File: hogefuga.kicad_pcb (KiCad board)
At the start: 2 copper layers, 95.3 x 97.6 mm, 45 parts, among them J1 MJ-4PP-9, SW1 SW_PUSH, SW10 SW_PUSH, SW11 SW_PUSH, SW12 SW_PUSH, SW13 SW_PUSH, SW14 SW_PUSH, SW15 SW_PUSH, SW16 SW_PUSH, SW17 SW_PUSH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

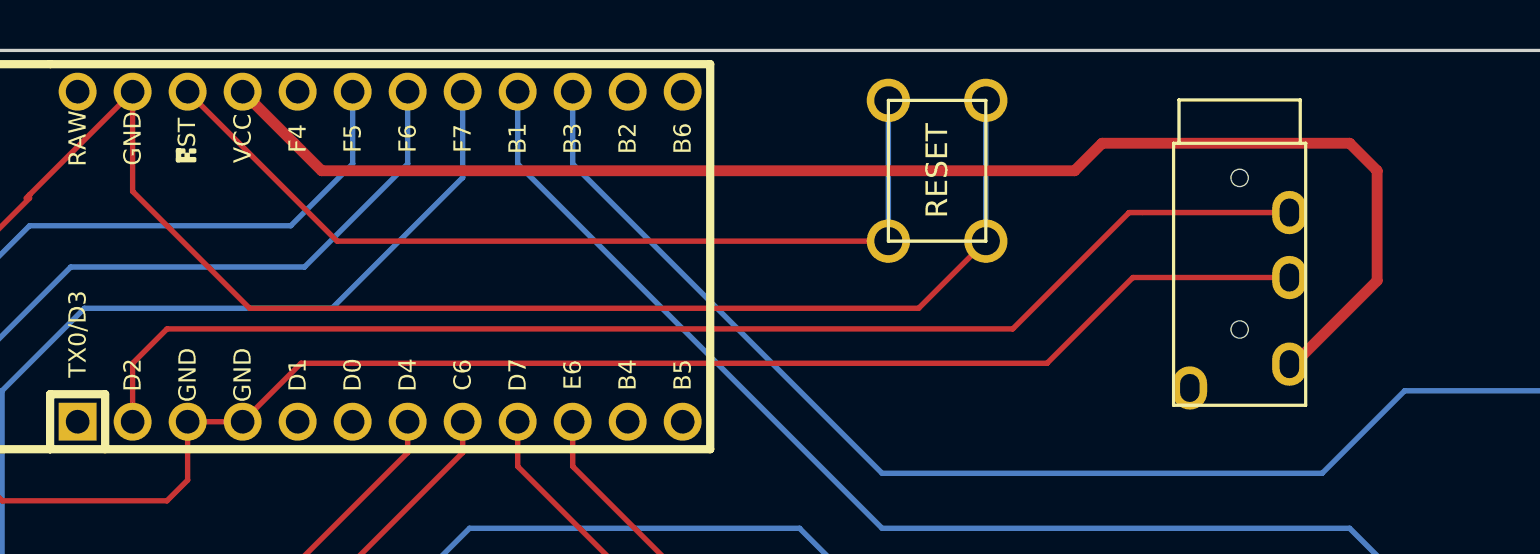
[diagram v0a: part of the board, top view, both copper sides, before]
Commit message: jack moved
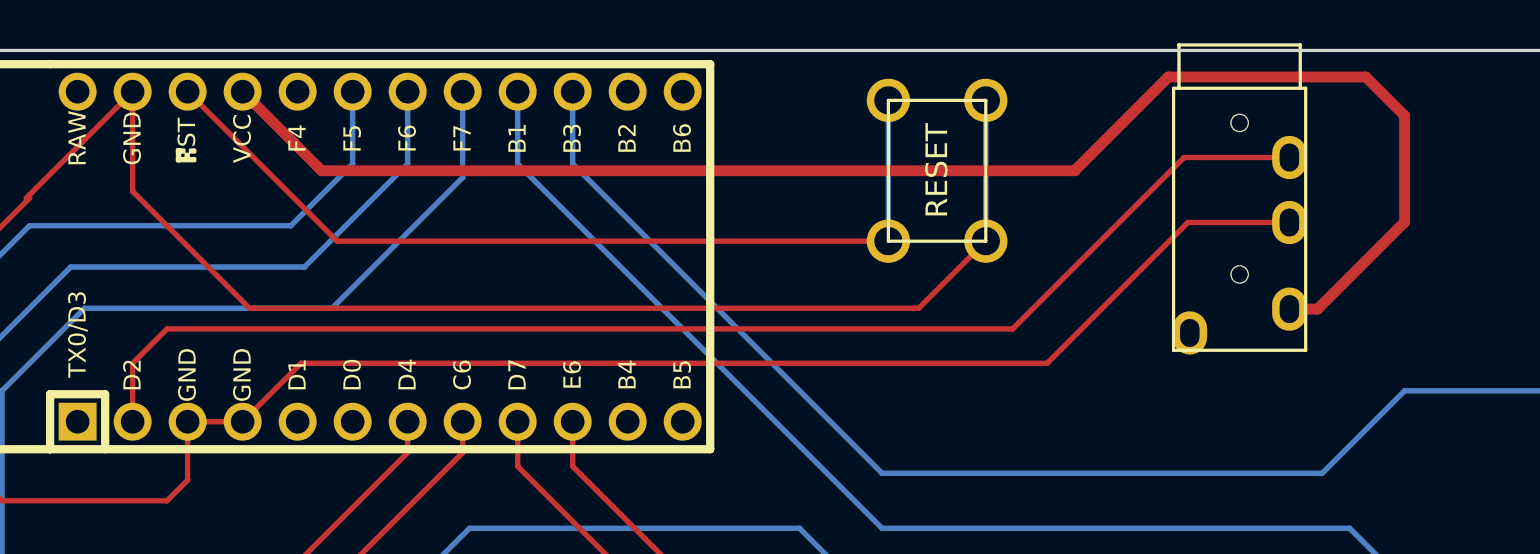
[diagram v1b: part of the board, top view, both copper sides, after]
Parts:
- moved J1 2.54 mm to (120.7, 27.9)
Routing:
- net VCC: track 65.7 -> 69.6 mm
- net data: track 59.0 -> 60.1 mm
- net GND: track 144.1 -> 145.1 mm
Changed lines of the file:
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@@
     (thickness 1.6)
     (drawings 10)
-    (tracks 372)
+    (tracks 371)
     (zones 0)
     (modules 45)
@@
   )
   (setup
-    (last_trace_width 0.25)
+    (last_trace_width 0.5)
     (user_trace_width 0.5)
     (trace_clearance 0.2)
@@
   )
   (module lib:Keebio-PJ-320A (layer F.Cu)
-    (at 120.65 30.48)
+    (at 120.65 27.94)
     (fp_text reference J1 (at 0 14.2) (layer Dwgs.User)
       (effects (font (size 1 1) (thickness 0.15)))
@@
   (segment (start 64.77 33.02) (end 59.69 38.1) (width 0.25) (layer F.Cu) (net 30))
   (segment (start 59.69 43.18) (end 59.69 38.1) (width 0.25) (layer F.Cu) (net 30))
-  (segment (start 115.72 36.68) (end 122.95 36.68) (width 0.25) (layer F.Cu) (net 30) (status 20))
   (segment (start 108.93 35) (end 108.93 28.5) (width 0.25) (layer B.Cu) (net 30))
-  (segment (start 74.6125 43.33875) (end 77.31125 40.64) (width 0.25) (layer F.Cu) (net 30))
-  (segment (start 77.31125 40.64) (end 111.76 40.64) (width 0.25) (layer F.Cu) (net 30))
-  (segment (start 111.76 40.64) (end 115.72 36.68) (width 0.25) (layer F.Cu) (net 30))
   (segment (start 69.5325 32.7025) (end 69.5325 28.09875) (width 0.25) (layer F.Cu) (net 30))
   (segment (start 74.93 38.1) (end 69.5325 32.7025) (width 0.25) (layer F.Cu) (net 30))
   (segment (start 108.93 35) (end 105.83 38.1) (width 0.25) (layer F.Cu) (net 30))
   (segment (start 105.83 38.1) (end 74.93 38.1) (width 0.25) (layer F.Cu) (net 30))
+  (segment (start 111.76 40.64) (end 118.26 34.14) (width 0.25) (layer F.Cu) (net 30))
+  (segment (start 118.26 34.14) (end 122.95 34.14) (width 0.25) (layer F.Cu) (net 30))
+  (segment (start 74.6125 43.33875) (end 77.31125 40.64) (width 0.25) (layer F.Cu) (net 30))
+  (segment (start 77.31125 40.64) (end 111.76 40.64) (width 0.25) (layer F.Cu) (net 30))
   (segment (start 78.26375 31.75) (end 76.99375 30.48) (width 0.5) (layer F.Cu) (net 33))
+  (segment (start 122.95 38.14) (end 124.25 38.14) (width 0.5) (layer F.Cu) (net 33))
+  (segment (start 76.99375 30.48) (end 74.6125 28.09875) (width 0.5) (layer F.Cu) (net 33))
+  (segment (start 126.479999 27.419999) (end 117.360001 27.419999) (width 0.5) (layer F.Cu) (net 33))
+  (segment (start 124.25 38.14) (end 128.27 34.12) (width 0.5) (layer F.Cu) (net 33))
   (segment (start 113.03 31.75) (end 78.26375 31.75) (width 0.5) (layer F.Cu) (net 33))
-  (segment (start 123.15 40.68) (end 127 36.83) (width 0.5) (layer F.Cu) (net 33))
-  (segment (start 122.95 40.68) (end 123.15 40.68) (width 0.5) (layer F.Cu) (net 33))
-  (segment (start 76.99375 30.48) (end 74.6125 28.09875) (width 0.5) (layer F.Cu) (net 33))
-  (segment (start 127 36.83) (end 127 31.75) (width 0.5) (layer F.Cu) (net 33))
-  (segment (start 127 31.75) (end 125.73 30.48) (width 0.5) (layer F.Cu) (net 33))
-  (segment (start 125.73 30.48) (end 114.3 30.48) (width 0.5) (layer F.Cu) (net 33))
-  (segment (start 114.3 30.48) (end 113.03 31.75) (width 0.5) (layer F.Cu) (net 33))
-  (segment (start 69.5325 40.64) (end 69.5325 43.33875) (width 0.25) (layer F.Cu) (net 40))
-  (segment (start 122.95 33.68) (end 116.18 33.68) (width 0.25) (layer F.Cu) (net 40))
+  (segment (start 128.27 34.12) (end 128.27 29.21) (width 0.5) (layer F.Cu) (net 33))
+  (segment (start 128.27 29.21) (end 126.479999 27.419999) (width 0.5) (layer F.Cu) (net 33))
+  (segment (start 117.360001 27.419999) (end 113.03 31.75) (width 0.5) (layer F.Cu) (net 33))
+  (segment (start 118.085 31.14) (end 122.95 31.14) (width 0.25) (layer F.Cu) (net 40))
   (segment (start 71.12 39.0525) (end 110.1725 39.0525) (width 0.25) (layer F.Cu) (net 40))
-  (segment (start 71.12 39.0525) (end 69.5325 40.64) (width 0.25) (layer F.Cu) (net 40))
-  (segment (start 115.545 33.68) (end 116.18 33.68) (width 0.25) (layer F.Cu) (net 40))
-  (segment (start 110.1725 39.0525) (end 115.545 33.68) (width 0.25) (layer F.Cu) (net 40))
+  (segment (start 69.5325 43.33875) (end 69.5325 40.64) (width 0.25) (layer F.Cu) (net 40))
+  (segment (start 110.1725 39.0525) (end 118.085 31.14) (width 0.25) (layer F.Cu) (net 40))
+  (segment (start 69.5325 40.64) (end 71.12 39.0525) (width 0.25) (layer F.Cu) (net 40))
 )

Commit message: GND塗りつぶし
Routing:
- added copper zone on B.Cu, net GND
- added copper zone on F.Cu, net GND
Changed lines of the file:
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@@
   (page A4)
   (layers
-    (0 F.Cu signal)
+    (0 F.Cu signal hide)
     (31 B.Cu signal)
     (32 B.Adhes user)
@@
   (segment (start 110.1725 39.0525) (end 118.085 31.14) (width 0.25) (layer F.Cu) (net 40))
   (segment (start 69.5325 40.64) (end 71.12 39.0525) (width 0.25) (layer F.Cu) (net 40))
+  (zone (net 30) (net_name GND) (layer F.Cu) (hatch edge 0.508)
+    (connect_pads (clearance 0.508))
+    (min_thickness 0.254)
+    (fill yes (arc_segments 16) (thermal_gap 0.508) (thermal_bridge_width 0.508))
+    (polygon
+      (pts
+        (xy 152.4 25.4) (xy 152.4 124.46) (xy 57.15 124.46) (xy 57.15 26.67) (xy 58.42 25.4)
+      )
+    )
+  )
+  (zone (net 30) (net_name GND) (layer B.Cu) (hatch edge 0.508)
+    (connect_pads (clearance 0.508))
+    (min_thickness 0.254)
+    (fill yes (arc_segments 16) (thermal_gap 0.508) (thermal_bridge_width 0.508))
+    (polygon
+      (pts
+        (xy 152.4 25.4) (xy 152.4 124.46) (xy 57.15 124.46) (xy 57.15 25.4)
+      )
+    )
+  )
 )

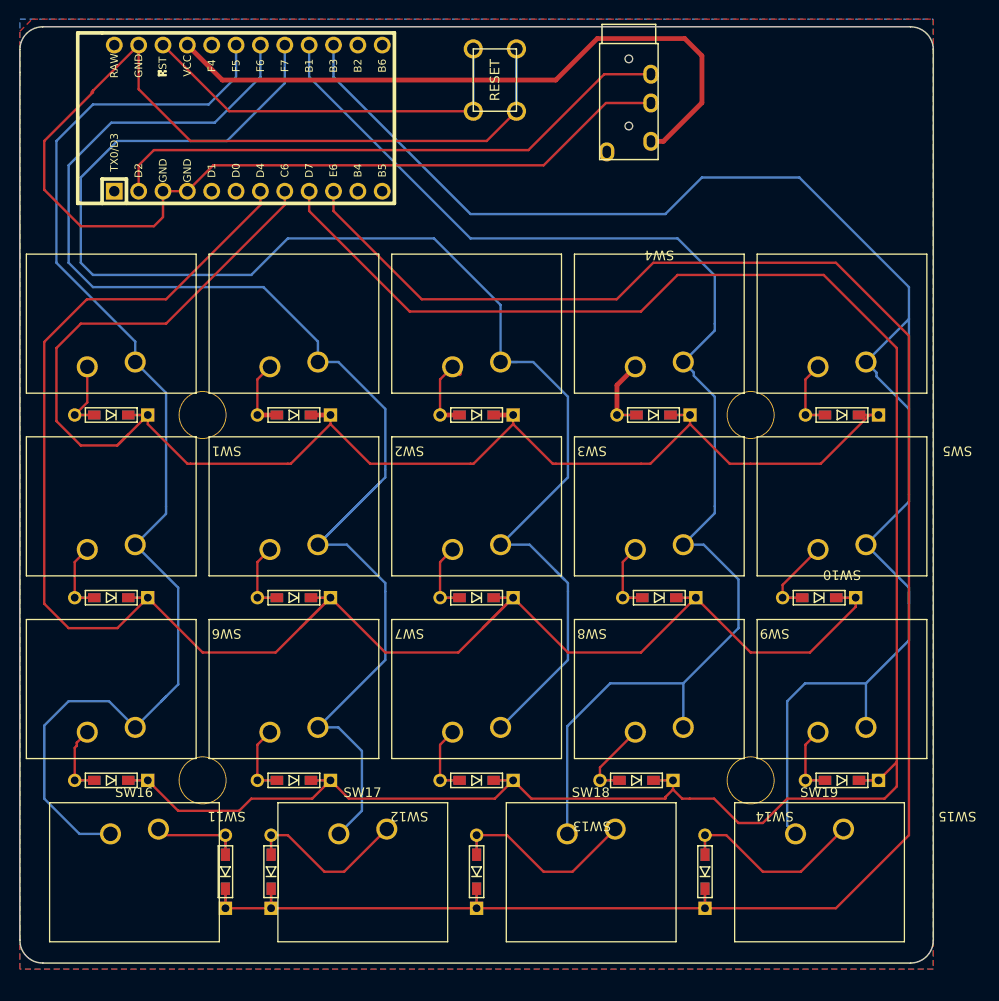
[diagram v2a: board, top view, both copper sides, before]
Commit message: bold GND, without 塗りつぶし
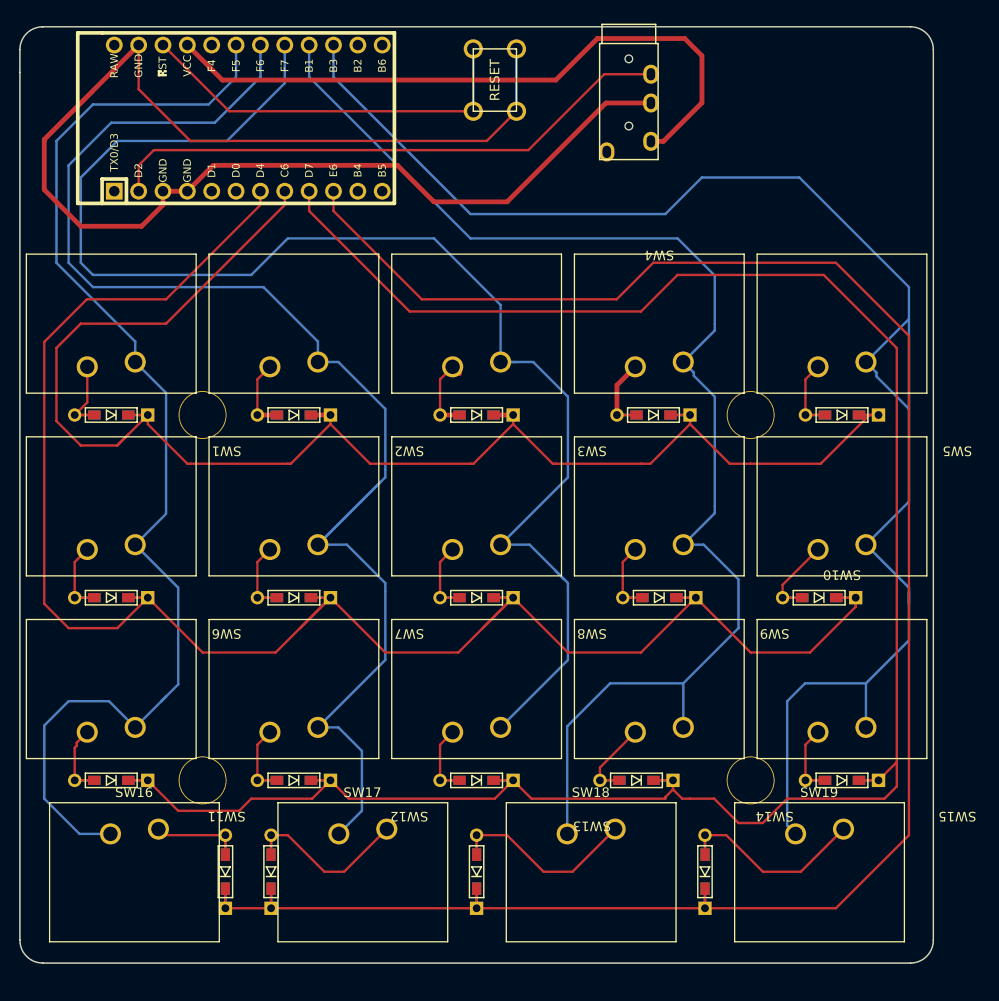
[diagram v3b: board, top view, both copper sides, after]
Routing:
- net GND: track 145.1 -> 161.6 mm
- removed copper zone on B.Cu, net GND
- removed copper zone on F.Cu, net GND
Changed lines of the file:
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@@
     (thickness 1.6)
     (drawings 10)
-    (tracks 371)
+    (tracks 375)
     (zones 0)
     (modules 45)
@@
   (page A4)
   (layers
-    (0 F.Cu signal hide)
+    (0 F.Cu signal)
     (31 B.Cu signal)
     (32 B.Adhes user)
@@
   (segment (start 72.0725 28.09875) (end 78.97375 35) (width 0.25) (layer F.Cu) (net 29))
   (segment (start 104.43 35) (end 104.43 28.5) (width 0.25) (layer B.Cu) (net 29))
-  (segment (start 72.0725 43.33875) (end 74.6125 43.33875) (width 0.25) (layer F.Cu) (net 30) (status 30))
-  (segment (start 72.0725 43.33875) (end 72.0725 46.0375) (width 0.25) (layer F.Cu) (net 30) (status 10))
-  (segment (start 72.0725 46.0375) (end 71.12 46.99) (width 0.25) (layer F.Cu) (net 30))
-  (segment (start 71.12 46.99) (end 63.5 46.99) (width 0.25) (layer F.Cu) (net 30))
-  (segment (start 63.5 46.99) (end 59.69 43.18) (width 0.25) (layer F.Cu) (net 30))
   (segment (start 64.77 32.86125) (end 64.77 33.02) (width 0.25) (layer F.Cu) (net 30))
   (segment (start 64.77 32.86125) (end 69.5325 28.09875) (width 0.25) (layer F.Cu) (net 30) (status 20))
   (segment (start 64.61125 33.02) (end 64.77 32.86125) (width 0.25) (layer F.Cu) (net 30))
   (segment (start 64.77 33.02) (end 59.69 38.1) (width 0.25) (layer F.Cu) (net 30))
-  (segment (start 59.69 43.18) (end 59.69 38.1) (width 0.25) (layer F.Cu) (net 30))
   (segment (start 108.93 35) (end 108.93 28.5) (width 0.25) (layer B.Cu) (net 30))
   (segment (start 69.5325 32.7025) (end 69.5325 28.09875) (width 0.25) (layer F.Cu) (net 30))
@@
   (segment (start 108.93 35) (end 105.83 38.1) (width 0.25) (layer F.Cu) (net 30))
   (segment (start 105.83 38.1) (end 74.93 38.1) (width 0.25) (layer F.Cu) (net 30))
-  (segment (start 111.76 40.64) (end 118.26 34.14) (width 0.25) (layer F.Cu) (net 30))
-  (segment (start 118.26 34.14) (end 122.95 34.14) (width 0.25) (layer F.Cu) (net 30))
-  (segment (start 74.6125 43.33875) (end 77.31125 40.64) (width 0.25) (layer F.Cu) (net 30))
-  (segment (start 77.31125 40.64) (end 111.76 40.64) (width 0.25) (layer F.Cu) (net 30))
+  (segment (start 96.52 40.64) (end 100.33 44.45) (width 0.5) (layer F.Cu) (net 30))
+  (segment (start 118.26 34.14) (end 122.95 34.14) (width 0.5) (layer F.Cu) (net 30))
+  (segment (start 107.95 44.45) (end 118.26 34.14) (width 0.5) (layer F.Cu) (net 30))
+  (segment (start 100.33 44.45) (end 107.95 44.45) (width 0.5) (layer F.Cu) (net 30))
+  (segment (start 74.6125 43.33875) (end 77.31125 40.64) (width 0.5) (layer F.Cu) (net 30))
+  (segment (start 77.31125 40.64) (end 96.52 40.64) (width 0.5) (layer F.Cu) (net 30))
+  (segment (start 74.6125 43.33875) (end 72.0725 43.33875) (width 0.5) (layer F.Cu) (net 30))
+  (segment (start 72.0725 43.33875) (end 72.0725 44.7675) (width 0.5) (layer F.Cu) (net 30))
+  (segment (start 72.0725 44.7675) (end 69.85 46.99) (width 0.5) (layer F.Cu) (net 30))
+  (segment (start 69.85 46.99) (end 63.5 46.99) (width 0.5) (layer F.Cu) (net 30))
+  (segment (start 63.5 46.99) (end 59.69 43.18) (width 0.5) (layer F.Cu) (net 30))
+  (segment (start 59.69 43.18) (end 59.69 38.1) (width 0.5) (layer F.Cu) (net 30))
+  (segment (start 59.69 37.94125) (end 69.5325 28.09875) (width 0.5) (layer F.Cu) (net 30))
+  (segment (start 59.69 38.1) (end 59.69 37.94125) (width 0.5) (layer F.Cu) (net 30))
   (segment (start 78.26375 31.75) (end 76.99375 30.48) (width 0.5) (layer F.Cu) (net 33))
   (segment (start 122.95 38.14) (end 124.25 38.14) (width 0.5) (layer F.Cu) (net 33))
@@
   (segment (start 110.1725 39.0525) (end 118.085 31.14) (width 0.25) (layer F.Cu) (net 40))
   (segment (start 69.5325 40.64) (end 71.12 39.0525) (width 0.25) (layer F.Cu) (net 40))
-  (zone (net 30) (net_name GND) (layer F.Cu) (hatch edge 0.508)
-    (connect_pads (clearance 0.508))
-    (min_thickness 0.254)
-    (fill yes (arc_segments 16) (thermal_gap 0.508) (thermal_bridge_width 0.508))
-    (polygon
-      (pts
-        (xy 152.4 25.4) (xy 152.4 124.46) (xy 57.15 124.46) (xy 57.15 26.67) (xy 58.42 25.4)
-      )
-    )
-  )
-  (zone (net 30) (net_name GND) (layer B.Cu) (hatch edge 0.508)
-    (connect_pads (clearance 0.508))
-    (min_thickness 0.254)
-    (fill yes (arc_segments 16) (thermal_gap 0.508) (thermal_bridge_width 0.508))
-    (polygon
-      (pts
-        (xy 152.4 25.4) (xy 152.4 124.46) (xy 57.15 124.46) (xy 57.15 25.4)
-      )
-    )
-  )
 )

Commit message: add credit
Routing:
- net col5: track 164.6 -> 155.2 mm
- added copper zone on B.Cu, net GND
- added copper zone on F.Cu, net GND
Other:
- board text added: "hogefuga v0.1 by yswallow"
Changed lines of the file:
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@@
   (general
     (thickness 1.6)
-    (drawings 10)
+    (drawings 11)
     (tracks 375)
     (zones 0)
@@
   (page A4)
   (layers
-    (0 F.Cu signal)
+    (0 F.Cu signal hide)
     (31 B.Cu signal)
     (32 B.Adhes user)
@@
   )
   (setup
-    (last_trace_width 0.5)
+    (last_trace_width 0.25)
     (user_trace_width 0.5)
     (trace_clearance 0.2)
@@
     )
     (pad "" np_thru_hole circle (at 0 0) (size 5 5) (drill 4.8) (layers *.Cu *.Mask))
+  )
+  (gr_text "hogefuga v0.1\nby yswallow" (at 146.05 33.02) (layer F.Mask)
+    (effects (font (size 1.5 1.5) (thickness 0.3)) (justify right))
   )
   (gr_arc (start 59.53125 121.44375) (end 57.15 121.44375) (angle -90) (layer Edge.Cuts) (width 0.15))
@@
   (segment (start 145.375 61.15) (end 146.474999 62.249999) (width 0.25) (layer B.Cu) (net 28))
   (segment (start 149.86 74.93) (end 149.86 66.04) (width 0.25) (layer B.Cu) (net 28))
-  (segment (start 149.86 66.04) (end 149.86 53.34) (width 0.25) (layer B.Cu) (net 28))
   (segment (start 145.375 80.2) (end 149.86 84.685) (width 0.25) (layer B.Cu) (net 28))
   (segment (start 149.86 84.685) (end 149.86 86.36) (width 0.25) (layer B.Cu) (net 28))
   (segment (start 149.86 85.09) (end 149.86 86.36) (width 0.25) (layer B.Cu) (net 28))
   (segment (start 149.86 86.36) (end 149.86 90.17) (width 0.25) (layer B.Cu) (net 28))
+  (segment (start 149.86 53.34) (end 149.86 56.665) (width 0.25) (layer B.Cu) (net 28))
   (segment (start 78.97375 35) (end 104.43 35) (width 0.25) (layer F.Cu) (net 29))
   (segment (start 72.0725 28.09875) (end 78.97375 35) (width 0.25) (layer F.Cu) (net 29))
@@
   (segment (start 110.1725 39.0525) (end 118.085 31.14) (width 0.25) (layer F.Cu) (net 40))
   (segment (start 69.5325 40.64) (end 71.12 39.0525) (width 0.25) (layer F.Cu) (net 40))
+  (zone (net 30) (net_name GND) (layer F.Cu) (hatch edge 0.508)
+    (connect_pads (clearance 0.508))
+    (min_thickness 0.254)
+    (fill yes (arc_segments 16) (thermal_gap 0.508) (thermal_bridge_width 0.508))
+    (polygon
+      (pts
+        (xy 152.4 25.4) (xy 152.4 124.46) (xy 57.15 125.73) (xy 57.15 25.4)
+      )
+    )
+  )
+  (zone (net 30) (net_name GND) (layer B.Cu) (hatch edge 0.508)
+    (connect_pads (clearance 0.508))
+    (min_thickness 0.254)
+    (fill yes (arc_segments 16) (thermal_gap 0.508) (thermal_bridge_width 0.508))
+    (polygon
+      (pts
+        (xy 152.4 25.4) (xy 152.4 124.46) (xy 57.15 124.46) (xy 57.15 25.4)
+      )
+    )
+  )
+  (zone (net 30) (net_name GND) (layer B.Cu) (hatch edge 0.508)
+    (connect_pads (clearance 0.508))
+    (min_thickness 0.254)
+    (fill yes (arc_segments 16) (thermal_gap 0.508) (thermal_bridge_width 0.508))
+    (polygon
+      (pts
+        (xy 152.4 55.88) (xy 152.4 67.31) (xy 143.51 67.31) (xy 143.51 55.88)
+      )
+    )
+  )
 )
